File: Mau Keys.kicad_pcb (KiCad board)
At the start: 2 copper layers, 36 parts

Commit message: hola2
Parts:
- NNV2: moved to B.Cu
- moved Switch11 49.5 mm to (38.2, 100.0)
- moved Switch1 49.5 mm to (25.3, 64.3)
- moved Switch10 49.5 mm to (113.0, 67.0)
- moved Switch13 49.5 mm to (75.0, 80.0)
- moved Switch14 49.5 mm to (94.0, 86.0)
- moved Switch15 49.5 mm to (113.0, 86.0)
- moved Switch16 49.5 mm to (103.5, 107.5)
- moved Switch3 49.5 mm to (75.0, 42.0)
- moved Switch4 49.5 mm to (94.0, 48.0)
- moved Switch5 49.5 mm to (113.0, 48.0)
- moved Switch6 49.5 mm to (31.7, 82.1)
- moved Switch7 49.5 mm to (52.2, 68.8)
- moved Switch8 49.5 mm to (75.0, 61.0)
- moved Switch9 49.5 mm to (94.0, 67.0)
- moved Switch12 49.5 mm to (55.5, 87.5)
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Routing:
- net S3: track 0.00 -> 64.8 mm

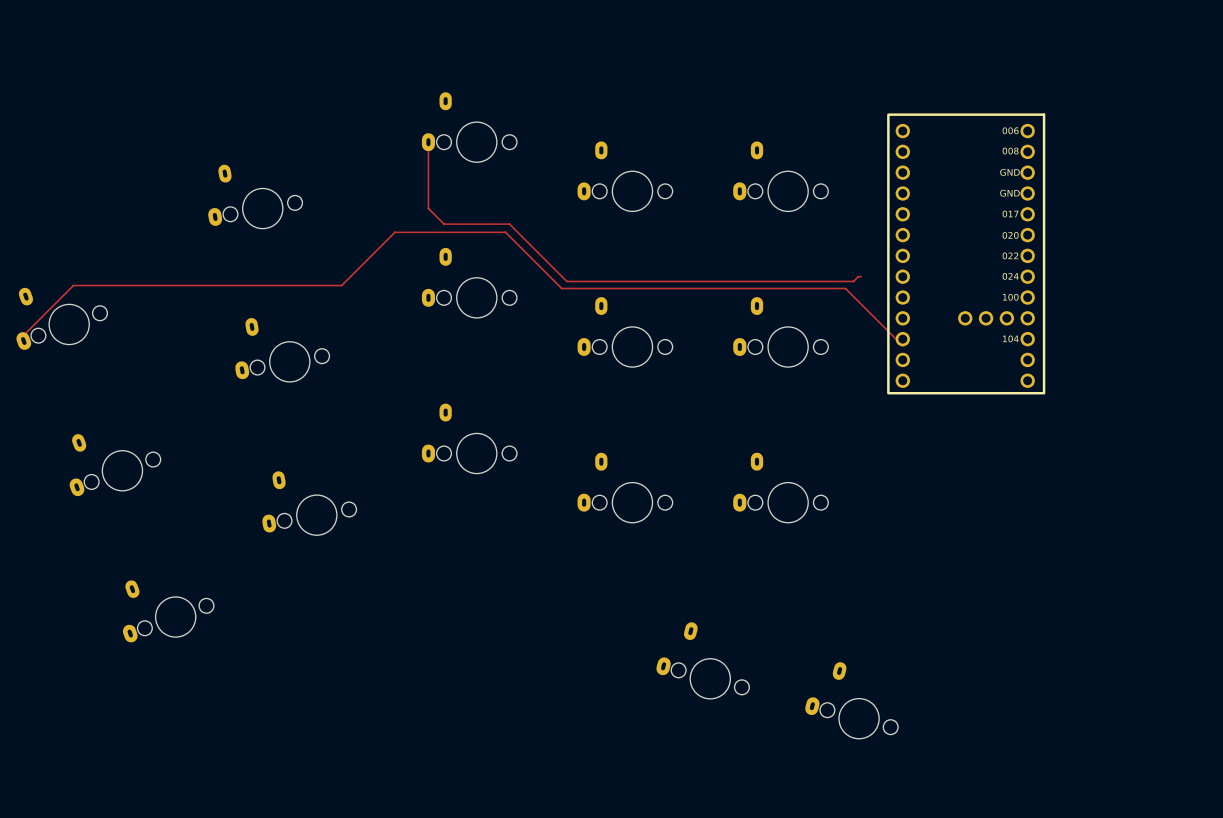
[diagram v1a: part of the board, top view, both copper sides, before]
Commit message: Add traces upper left
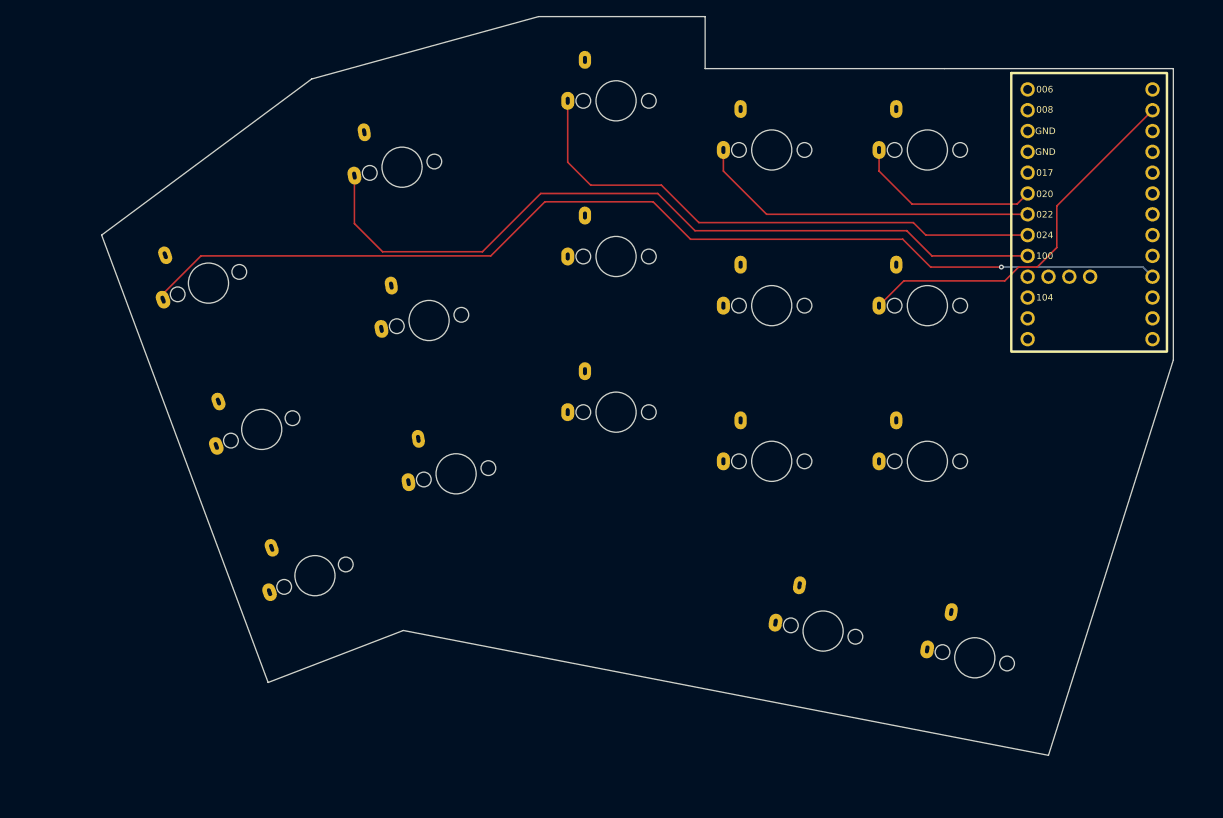
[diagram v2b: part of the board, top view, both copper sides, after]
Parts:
- NNV2: moved to F.Cu
- moved Switch10 17.7 mm to (130.0, 62.0)
- moved Switch13 17.7 mm to (92.0, 75.0)
- moved Switch14 17.7 mm to (111.0, 81.0)
- moved Switch15 17.7 mm to (130.0, 81.0)
- moved Switch3 17.7 mm to (92.0, 37.0)
- moved Switch4 17.7 mm to (111.0, 43.0)
- moved Switch5 17.7 mm to (130.0, 43.0)
- moved Switch6 17.7 mm to (48.7, 77.1)
- moved Switch7 17.7 mm to (69.2, 63.8)
- moved Switch8 17.7 mm to (92.0, 56.0)
- moved Switch9 17.7 mm to (111.0, 62.0)
- moved Switch1 17.7 mm to (42.3, 59.2)
- moved Switch12 17.7 mm to (72.5, 82.5)
- moved Switch2 17.7 mm to (65.9, 45.1)
- moved Switch11 17.7 mm to (55.2, 94.9)
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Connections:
- NNV2 pad 1: GND -> VBAT
- NNV2 pad 10: S1 -> S6
- NNV2 pad 11: S15 -> S7
- NNV2 pad 12: S16 -> S8
- NNV2 pad 13: S17 -> S9
- NNV2 pad 14: VBAT -> GND
- NNV2 pad 15: VBAT -> S10
- NNV2 pad 16: GND -> unconnected-(NNV2-Pad16)
- NNV2 pad 17: RESET -> GND
- NNV2 pad 18: EXT_VCC -> GND
- NNV2 pad 19: S5 -> S11
- NNV2 pad 2: S10 -> VBAT
- NNV2 pad 20: S4 -> S12
- NNV2 pad 21: S3 -> S13
- NNV2 pad 22: S2 -> S14
- NNV2 pad 23: S6 -> S1
- NNV2 pad 24: S7 -> S15
- NNV2 pad 25: S8 -> S16
- NNV2 pad 26: S9 -> S17
- NNV2 pad 3: unconnected-(NNV2-Pad3) -> GND
- NNV2 pad 4: GND -> RESET
- NNV2 pad 5: GND -> EXT_VCC
- NNV2 pad 6: S11 -> S5
- NNV2 pad 7: S12 -> S4
- NNV2 pad 8: S13 -> S3
- NNV2 pad 9: S14 -> S2
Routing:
- net S2: track 0.00 -> 95.6 mm
- net S10: track 0.00 -> 46.2 mm
- net S4: track 0.00 -> 41.9 mm
- net S5: track 0.00 -> 22.9 mm
- net S1: track 119.0 -> 129.9 mm, vias 0 -> 1
- net S3: track 64.8 -> 67.3 mm
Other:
- board outline added: 130.8 x 90.2 mm

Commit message: Traces upper left
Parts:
- removed SwitchR_17: ~, Switches:keyswitch_cherrymx_alps_choc12_slots_1u
- added Switch17: ~, Switches:keyswitch_cherrymx_alps_choc12_slots_1u, F.Cu at (140.0, 106.7)
- moved NNV2_R1 67.8 mm to (172.1, 41.4)
- moved Switch2 5.06 mm to (66.0, 40.0), turned to 5 degrees
- moved Switch11 4.54 mm to (51.4, 97.4), turned to 10 degrees
- moved Switch7 4.10 mm to (67.7, 59.9), turned to 5 degrees
- moved Switch12 3.98 mm to (69.5, 79.8), turned to 5 degrees
- moved Switch3 3.57 mm to (90.0, 34.0)
- moved Switch16 2.98 mm to (119.1, 104.0), turned to -5 degrees
- moved Switch8 2.79 mm to (90.0, 54.0)
- moved Switch1 2.55 mm to (44.5, 58.0), turned to 10 degrees
- moved Switch14 2.28 mm to (110.0, 83.0)
- moved Switch13 2.22 mm to (90.0, 74.0)
- moved Switch15 2.05 mm to (130.0, 83.0)
- moved Switch9 1.45 mm to (110.0, 63.0)
- moved Switch10 1.05 mm to (130.0, 63.0)
- moved Switch6 1.01 mm to (48.0, 77.7), turned to 10 degrees
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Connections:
- NNV2 pad 1: VBAT -> GND
- NNV2 pad 10: S6 -> S7
- NNV2 pad 11: S7 -> S8
- NNV2 pad 12: S8 -> S9
- NNV2 pad 13: S9 -> S10
- NNV2 pad 14: GND -> VBAT
- NNV2 pad 15: S10 -> VBAT
- NNV2 pad 16: unconnected-(NNV2-Pad16) -> GND
- NNV2 pad 17: GND -> RESET
- NNV2 pad 18: GND -> EXT_VCC
- NNV2 pad 2: VBAT -> S1
- NNV2 pad 23: S1 -> S15
- NNV2 pad 24: S15 -> S16
- NNV2 pad 25: S16 -> S17
- NNV2 pad 26: S17 -> unconnected-(NNV2-Pad26)
- NNV2 pad 3: GND -> S2
- NNV2 pad 4: RESET -> GND
- NNV2 pad 5: EXT_VCC -> GND
- NNV2 pad 6: S5 -> S3
- NNV2 pad 8: S3 -> S5
- NNV2 pad 9: S2 -> S6
- NNV2_R1 pad 10: S1_R -> S15_R
- NNV2_R1 pad 11: S15_R -> S16_R
- NNV2_R1 pad 12: S16_R -> S17_R
- NNV2_R1 pad 13: S17_R -> unconnected-(NNV2_R1-Pad13)
- NNV2_R1 pad 19: S5_R -> S1_R
- NNV2_R1 pad 2: S10_R -> S7_R
- NNV2_R1 pad 20: S4_R -> S2_R
- NNV2_R1 pad 22: S2_R -> S4_R
- NNV2_R1 pad 23: S6_R -> S5_R
- NNV2_R1 pad 24: S7_R -> S6_R
- NNV2_R1 pad 26: S9_R -> S10_R
- NNV2_R1 pad 3: unconnected-(NNV2_R1-Pad3) -> S9_R
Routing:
- net S10: track 46.2 -> 0.00 mm
- net S5: track 22.9 -> 38.1 mm
- net S4: track 41.9 -> 56.2 mm
- net S3: track 67.3 -> 79.5 mm
- net S2: track 95.6 -> 99.1 mm
- net S1: track 129.9 -> 132.4 mm, vias 1 -> 0
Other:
- board outline removed

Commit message: dxf de teclado
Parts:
- removed NNV2: ~, Microcontroller:nice_nano
- removed Switch1, Switch11, Switch12, Switch2, Switch6, Switch7: ~, Switches:keyswitch_cherrymx_alps_choc12_slots_1u
- added NNV2_R1: ~, Microcontroller:nice_nano, F.Cu at (149.6, 30.0)
- added Switch13: ~, Switches:keyswitch_cherrymx_alps_choc12_slots_1u, F.Cu at (70.0, 69.0)
- added Switch13: ~, Switches:keyswitch_cherrymx_alps_choc12_slots_1u, F.Cu at (52.0, 86.0)
- added Switch3: ~, Switches:keyswitch_cherrymx_alps_choc12_slots_1u, F.Cu at (66.5, 29.2)
- added Switch3: ~, Switches:keyswitch_cherrymx_alps_choc12_slots_1u, F.Cu at (43.7, 46.9)
- added Switch8: ~, Switches:keyswitch_cherrymx_alps_choc12_slots_1u, F.Cu at (47.8, 66.4)
- added Switch8: ~, Switches:keyswitch_cherrymx_alps_choc12_slots_1u, F.Cu at (68.3, 49.1)
- moved SwitchR_6 30.6 mm to (237.0, 72.0)
- moved SwitchR_13 24.6 mm to (256.0, 75.0)
- moved Switch13 17.0 mm to (90.0, 57.0)
- moved Switch3 17.0 mm to (90.0, 17.0)
- moved Switch8 17.0 mm to (90.0, 37.0)
- moved NNV2_R1 16.8 mm to (187.6, 35.1)
- moved Switch17 16.5 mm to (154.0, 98.0)
- moved Switch14 16.0 mm to (110.0, 67.0)
- moved Switch4 16.0 mm to (110.0, 27.0)
- moved Switch9 16.0 mm to (110.0, 47.0)
- moved Switch16 14.0 mm to (119.0, 90.0)
- moved Switch17 13.3 mm to (230.0, 109.8)
- moved SwitchR_1 13.3 mm to (230.0, 119.3)
- moved SwitchR_10 13.3 mm to (242.6, 138.4)
- moved SwitchR_11 13.3 mm to (242.6, 147.9)
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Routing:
- net S1: track 132.4 -> 0.00 mm
- net S2: track 99.1 -> 0.00 mm
- net S3: track 79.5 -> 0.00 mm
- net S4: track 56.2 -> 0.00 mm
- net S5: track 38.1 -> 0.00 mm
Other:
- board outline added: 127.6 x 102.7 mm

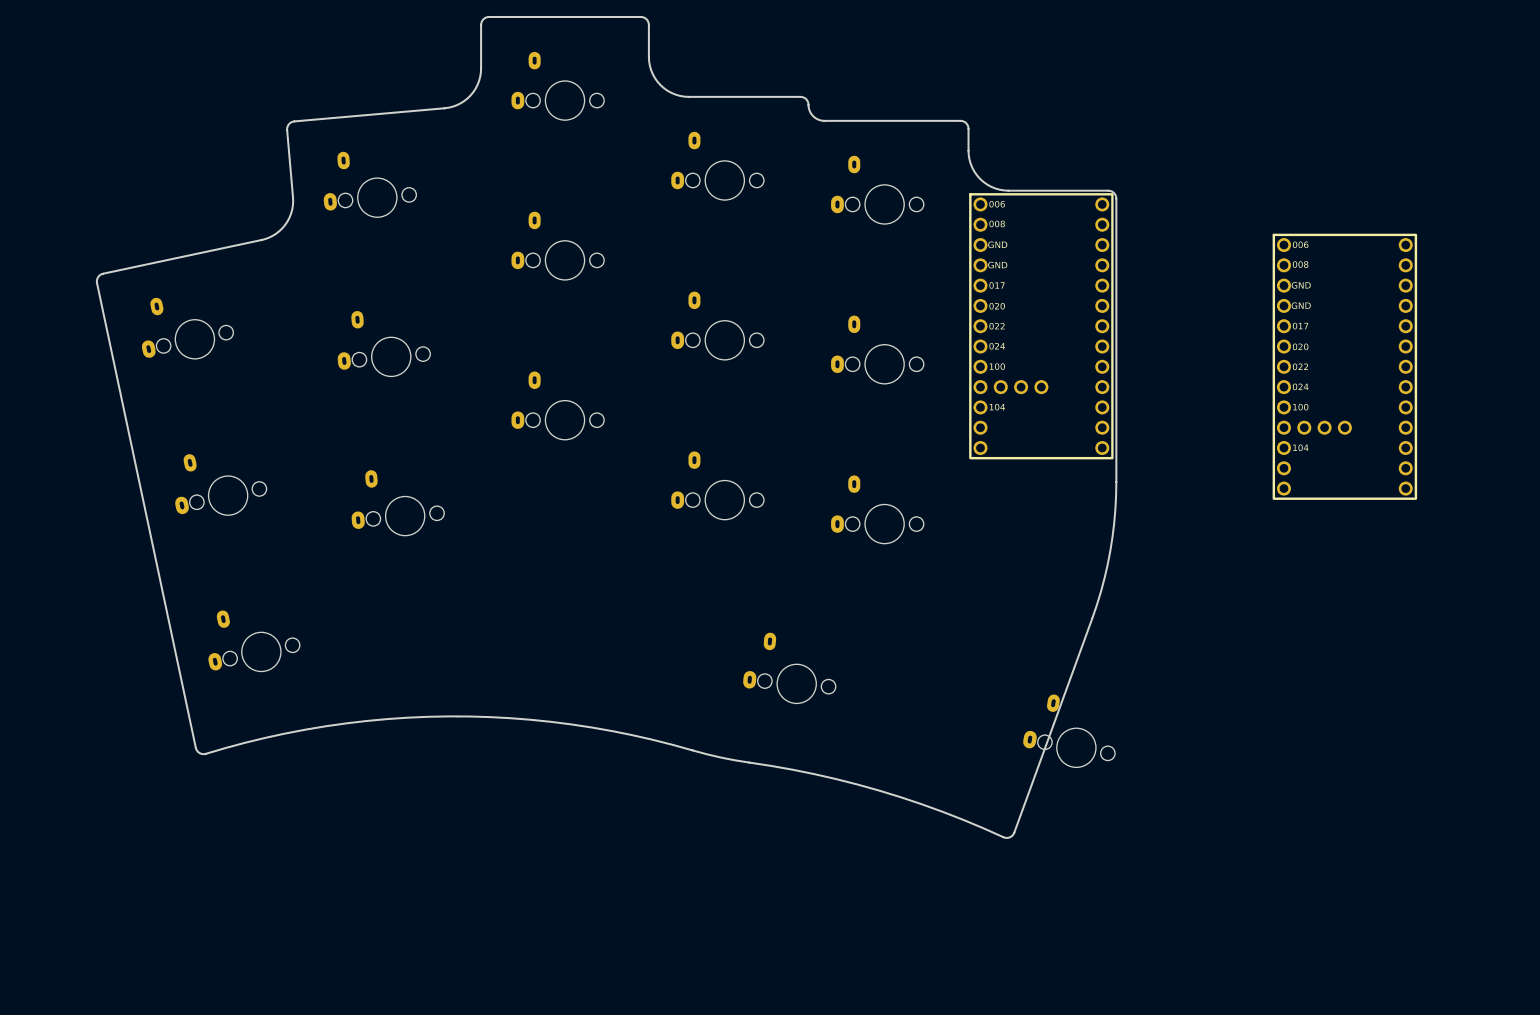
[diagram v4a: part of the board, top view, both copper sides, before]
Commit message: traces lado izquierdo
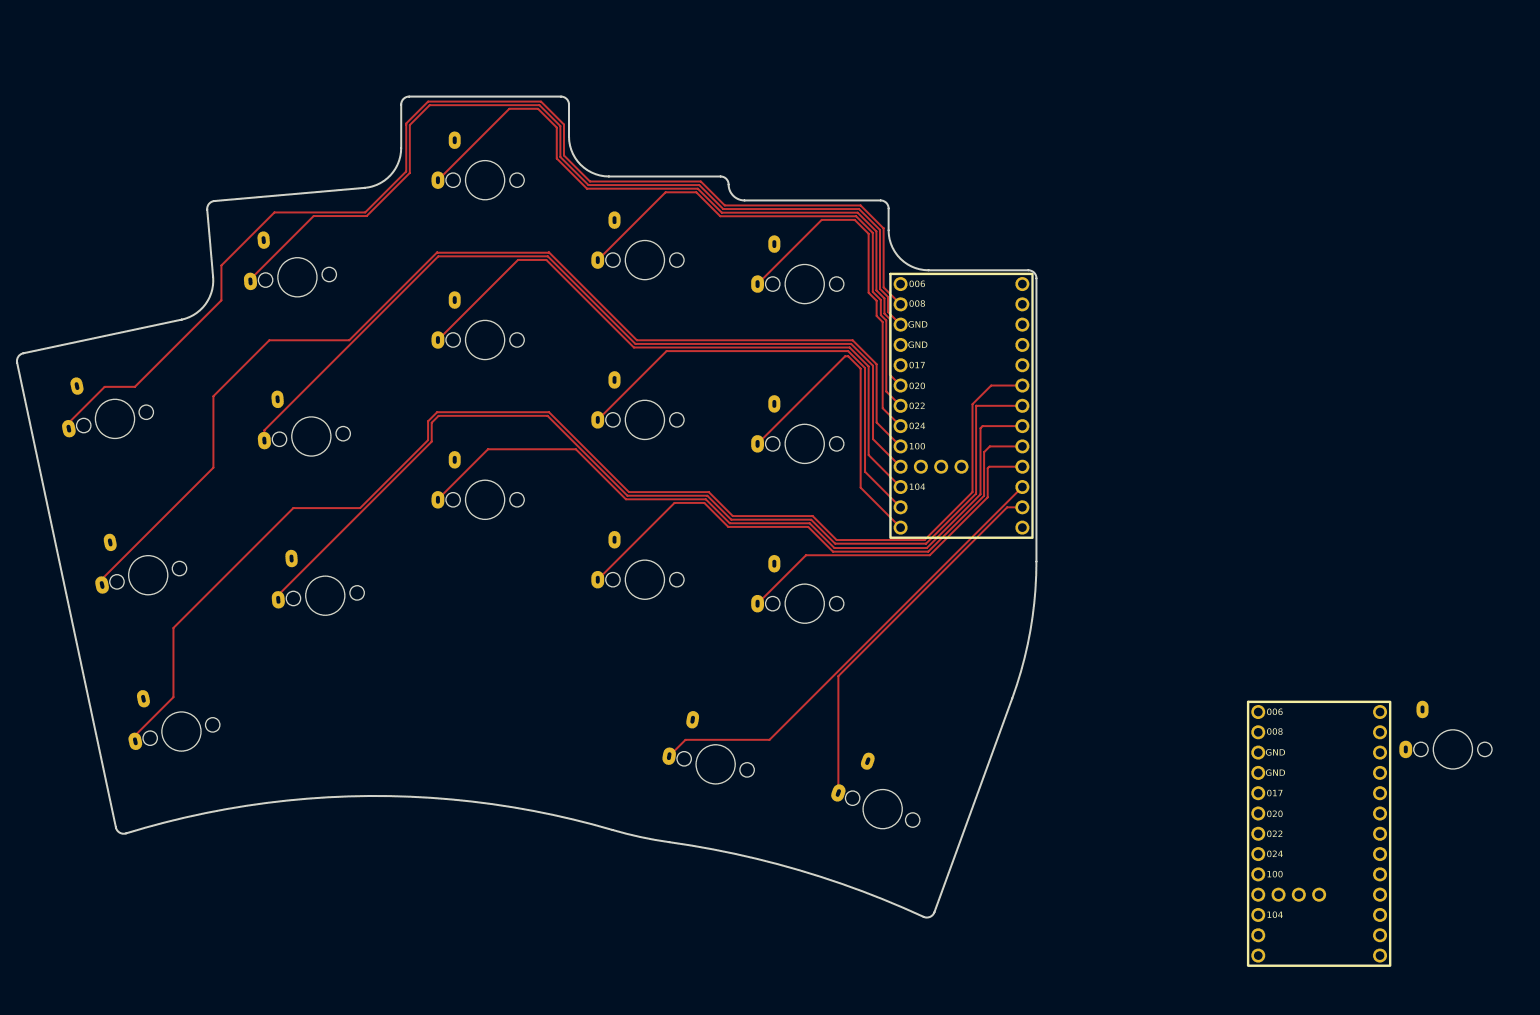
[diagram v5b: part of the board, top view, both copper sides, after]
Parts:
- added SwitchR_17: ~, Switches:keyswitch_cherrymx_alps_choc12_slots_1u, F.Cu at (201.1, 98.2)
- moved NNV2_R1 58.5 mm to (184.4, 93.5)
- moved Switch17 25.4 mm to (129.8, 105.7), turned to -20 degrees
- moved Switch16 14.3 mm to (108.9, 100.1), turned to -10 degrees
- moved NNV2 14.1 mm to (139.6, 40.0)
- moved Switch10 14.1 mm to (120.0, 60.0)
- moved Switch11 14.1 mm to (42.0, 96.0)
- moved Switch12 14.1 mm to (60.0, 79.0)
- moved Switch13 14.1 mm to (80.0, 67.0)
- moved Switch14 14.1 mm to (100.0, 77.0)
- moved Switch15 14.1 mm to (120.0, 80.0)
- moved Switch4 14.1 mm to (100.0, 37.0)
- moved Switch5 14.1 mm to (120.0, 40.0)
- moved Switch8 14.1 mm to (80.0, 47.0)
- moved Switch9 14.1 mm to (100.0, 57.0)
- moved Switch3 14.1 mm to (80.0, 27.0)
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- renumbered NNV2_R1 to NNV2, Switch3 to Switch1, Switch13 to Switch11, Switch13 to Switch12, Switch3 to Switch2, Switch8 to Switch6, Switch8 to Switch7
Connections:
- NNV2 pad 1: (no net) -> GND
- NNV2 pad 10: (no net) -> S7
- NNV2 pad 11: (no net) -> S8
- NNV2 pad 12: (no net) -> S9
- NNV2 pad 13: (no net) -> S10
- NNV2 pad 14: (no net) -> VBAT
- NNV2 pad 15: (no net) -> VBAT
- NNV2 pad 16: (no net) -> GND
- NNV2 pad 17: (no net) -> RESET
- NNV2 pad 18: (no net) -> EXT_VCC
- NNV2 pad 19: (no net) -> S11
- NNV2 pad 2: (no net) -> S1
- NNV2 pad 20: (no net) -> S12
- NNV2 pad 21: (no net) -> S13
- NNV2 pad 22: (no net) -> S14
- NNV2 pad 23: (no net) -> S15
- NNV2 pad 24: (no net) -> S16
- NNV2 pad 25: (no net) -> S17
- NNV2 pad 26: (no net) -> unconnected-(NNV2-Pad26)
- NNV2 pad 27: (no net) -> unconnected-(NNV2-Pad27)
- NNV2 pad 28: (no net) -> unconnected-(NNV2-Pad28)
- NNV2 pad 29: (no net) -> unconnected-(NNV2-Pad29)
- NNV2 pad 3: (no net) -> S2
- NNV2 pad 4: (no net) -> GND
- NNV2 pad 5: (no net) -> GND
- NNV2 pad 6: (no net) -> S3
- NNV2 pad 7: (no net) -> S4
- NNV2 pad 8: (no net) -> S5
- NNV2 pad 9: (no net) -> S6
- Switch1 pad 1: S3 -> S1
- Switch11 pad 1: S13 -> S11
- Switch12 pad 1: S13 -> S12
- Switch2 pad 1: S3 -> S2
- Switch6 pad 1: S8 -> S6
- Switch7 pad 1: S8 -> S7
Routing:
- net S11: track 0.00 -> 156.1 mm
- net S1: track 0.00 -> 144.7 mm
- net S6: track 0.00 -> 137.2 mm
- net S12: track 0.00 -> 124.6 mm
- net S2: track 0.00 -> 113.2 mm
- net S7: track 0.00 -> 106.2 mm
- net S13: track 0.00 -> 92.1 mm
- net S3: track 0.00 -> 87.7 mm
- net S8: track 0.00 -> 80.3 mm
- net S14: track 0.00 -> 68.3 mm
- net S4: track 0.00 -> 63.1 mm
- net S16: track 0.00 -> 58.2 mm
- net S9: track 0.00 -> 57.2 mm
- net S17: track 0.00 -> 46.4 mm
- net S5: track 0.00 -> 43.7 mm
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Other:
- board text removed: "10°"

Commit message: finished left
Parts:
- added NNV2: ~, Microcontroller:nice_nano, F.Cu at (153.4, 157.4)
- added NNV2: ~, Microcontroller:nice_nano, B.Cu at (160.2, 40.3)
- added RSW1: SW_Push, reset:SW_RESET, F.Cu at (145.2, 74.5)
- added RSW1: SW_Push, reset:SW_RESET, F.Cu at (159.0, 192.0)
- added RSW2: SW_Push, reset:SW_RESET, F.Cu at (164.0, 23.8)
- added SW_POWER1: SW_SPDT, switch_button:smt-slider-switch, B.Cu at (139.6, 40.0)
- added SW_POWER1: SW_SPDT, switch_button:smt-slider-switch, B.Cu at (153.4, 157.4)
- added SW_POWER2: SW_SPDT, switch_button:smt-slider-switch, F.Cu at (155.8, 28.9)
- added Switch1: ~, Switches:keyswitch_cherrymx_alps_choc12_slots_1u, F.Cu at (47.5, 174.3)
- added Switch10: ~, Switches:keyswitch_cherrymx_alps_choc12_slots_1u, F.Cu at (194.8, 53.5)
- added Switch10: ~, Switches:keyswitch_cherrymx_alps_choc12_slots_1u, F.Cu at (133.8, 177.4)
- added Switch11: ~, Switches:keyswitch_cherrymx_alps_choc12_slots_1u, F.Cu at (55.8, 213.4)
- added Switch12: ~, Switches:keyswitch_cherrymx_alps_choc12_slots_1u, F.Cu at (73.8, 196.4)
- added Switch13: ~, Switches:keyswitch_cherrymx_alps_choc12_slots_1u, F.Cu at (93.8, 184.4)
- added Switch14: ~, Switches:keyswitch_cherrymx_alps_choc12_slots_1u, F.Cu at (113.8, 194.4)
- added Switch14: ~, Switches:keyswitch_cherrymx_alps_choc12_slots_1u, F.Cu at (214.8, 70.5)
- added Switch15: ~, Switches:keyswitch_cherrymx_alps_choc12_slots_1u, F.Cu at (133.8, 197.4)
- added Switch15: ~, Switches:keyswitch_cherrymx_alps_choc12_slots_1u, F.Cu at (194.8, 73.5)
- added Switch16: ~, Switches:keyswitch_cherrymx_alps_choc12_slots_1u, F.Cu at (122.6, 217.5)
- added Switch17: ~, Switches:keyswitch_cherrymx_alps_choc12_slots_1u, F.Cu at (143.5, 223.1)
- added Switch2: ~, Switches:keyswitch_cherrymx_alps_choc12_slots_1u, F.Cu at (70.3, 156.6)
- added Switch3: ~, Switches:keyswitch_cherrymx_alps_choc12_slots_1u, F.Cu at (93.8, 144.4)
- added Switch4: ~, Switches:keyswitch_cherrymx_alps_choc12_slots_1u, F.Cu at (113.8, 154.4)
- added Switch4: ~, Switches:keyswitch_cherrymx_alps_choc12_slots_1u, F.Cu at (214.8, 30.5)
- added Switch5: ~, Switches:keyswitch_cherrymx_alps_choc12_slots_1u, F.Cu at (133.8, 157.4)
- added Switch5: ~, Switches:keyswitch_cherrymx_alps_choc12_slots_1u, F.Cu at (194.8, 33.5)
- added Switch6: ~, Switches:keyswitch_cherrymx_alps_choc12_slots_1u, F.Cu at (51.6, 193.9)
- added Switch7: ~, Switches:keyswitch_cherrymx_alps_choc12_slots_1u, F.Cu at (72.0, 176.5)
- added Switch8: ~, Switches:keyswitch_cherrymx_alps_choc12_slots_1u, F.Cu at (93.8, 164.4)
- added Switch9: ~, Switches:keyswitch_cherrymx_alps_choc12_slots_1u, F.Cu at (113.8, 174.4)
- added Switch9: ~, Switches:keyswitch_cherrymx_alps_choc12_slots_1u, F.Cu at (214.8, 50.5)
- moved NNV2_R1 16.4 mm to (172.2, 104.5)
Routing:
- net S11: track 156.1 -> 305.3 mm
- net S1: track 144.7 -> 289.4 mm
- net S6: track 137.2 -> 274.3 mm
- net S12: track 124.6 -> 240.2 mm
- net S2: track 113.2 -> 226.5 mm
- net S7: track 106.2 -> 212.4 mm
- net S3: track 87.7 -> 175.5 mm
- net S13: track 92.1 -> 178.9 mm
- net S8: track 80.3 -> 160.6 mm
- net S14: track 68.3 -> 133.0 mm
- net S4: track 63.1 -> 126.2 mm
- net RESET: track 0.00 -> 59.9 mm, vias 0 -> 4
- net S16: track 58.2 -> 116.3 mm
- net S9: track 57.2 -> 114.3 mm
- net S17: track 46.4 -> 95.1 mm
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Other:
- board size 127.6 x 102.7 mm -> 257 x 220.2 mm
